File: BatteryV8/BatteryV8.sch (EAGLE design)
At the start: 69 parts, among them IC1 MAX6462XR29T, Q1 MOSFET-PCHANNEL, Q2 MOSFET-PCHANNEL, Q3 MOSFET-PCHANNEL, X1 MINI-USB-UX60-MB-5ST

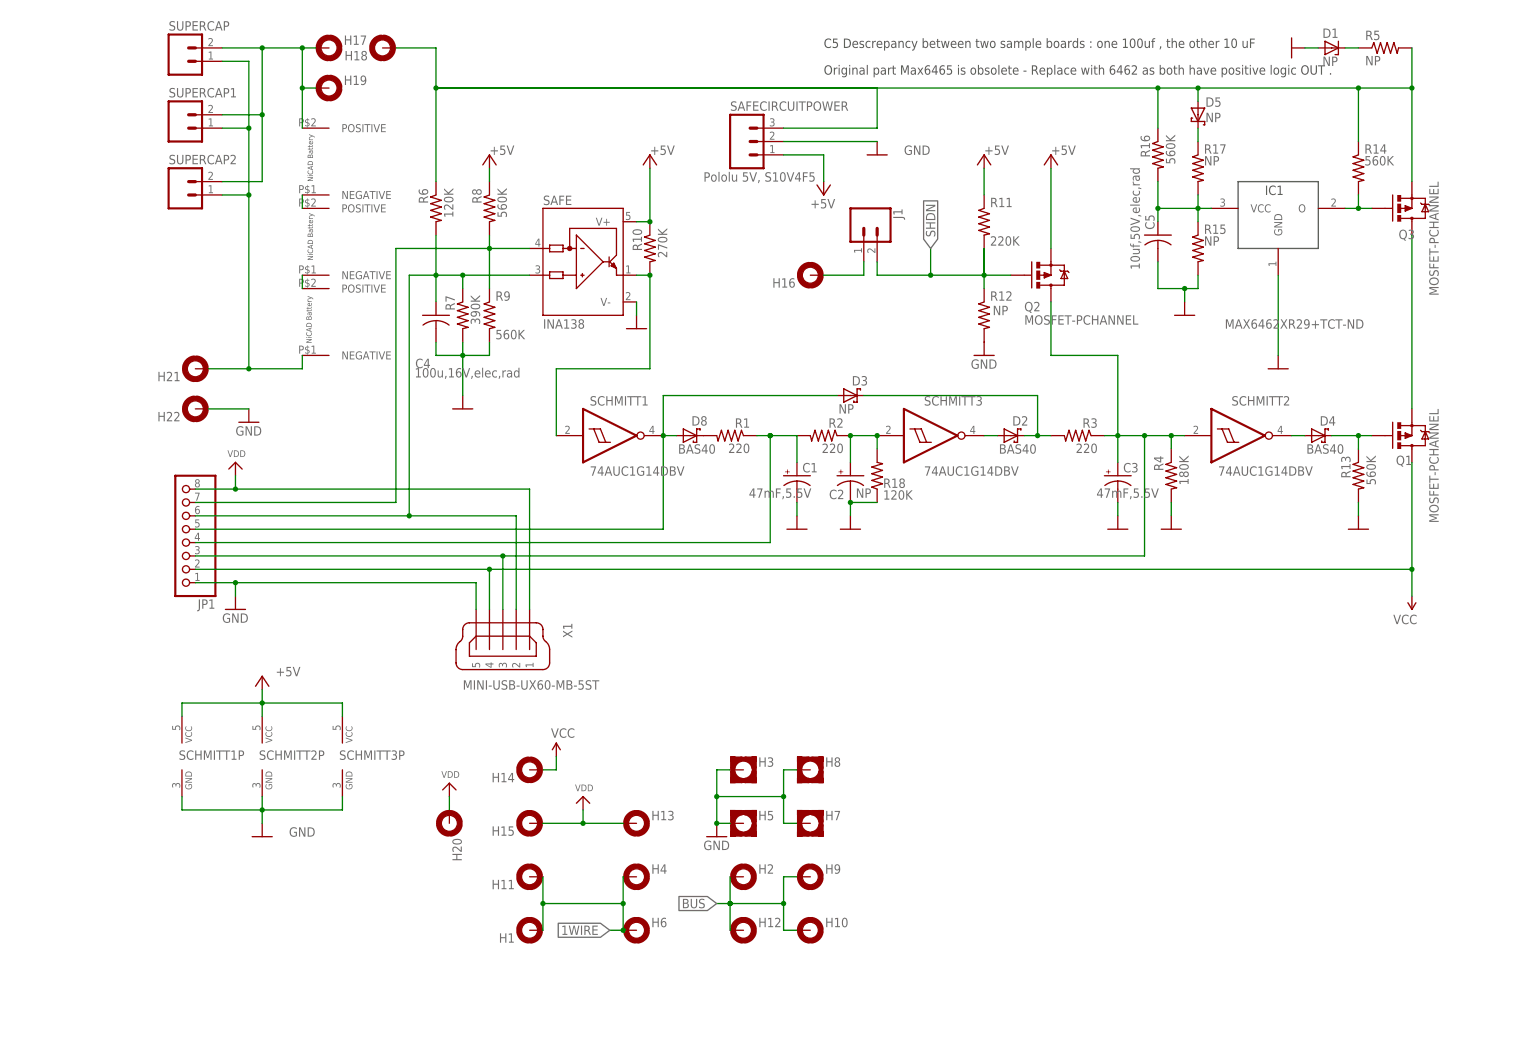
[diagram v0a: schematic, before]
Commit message: updated schematics and BOM with notes in the course of assembling the 3 main PCBs
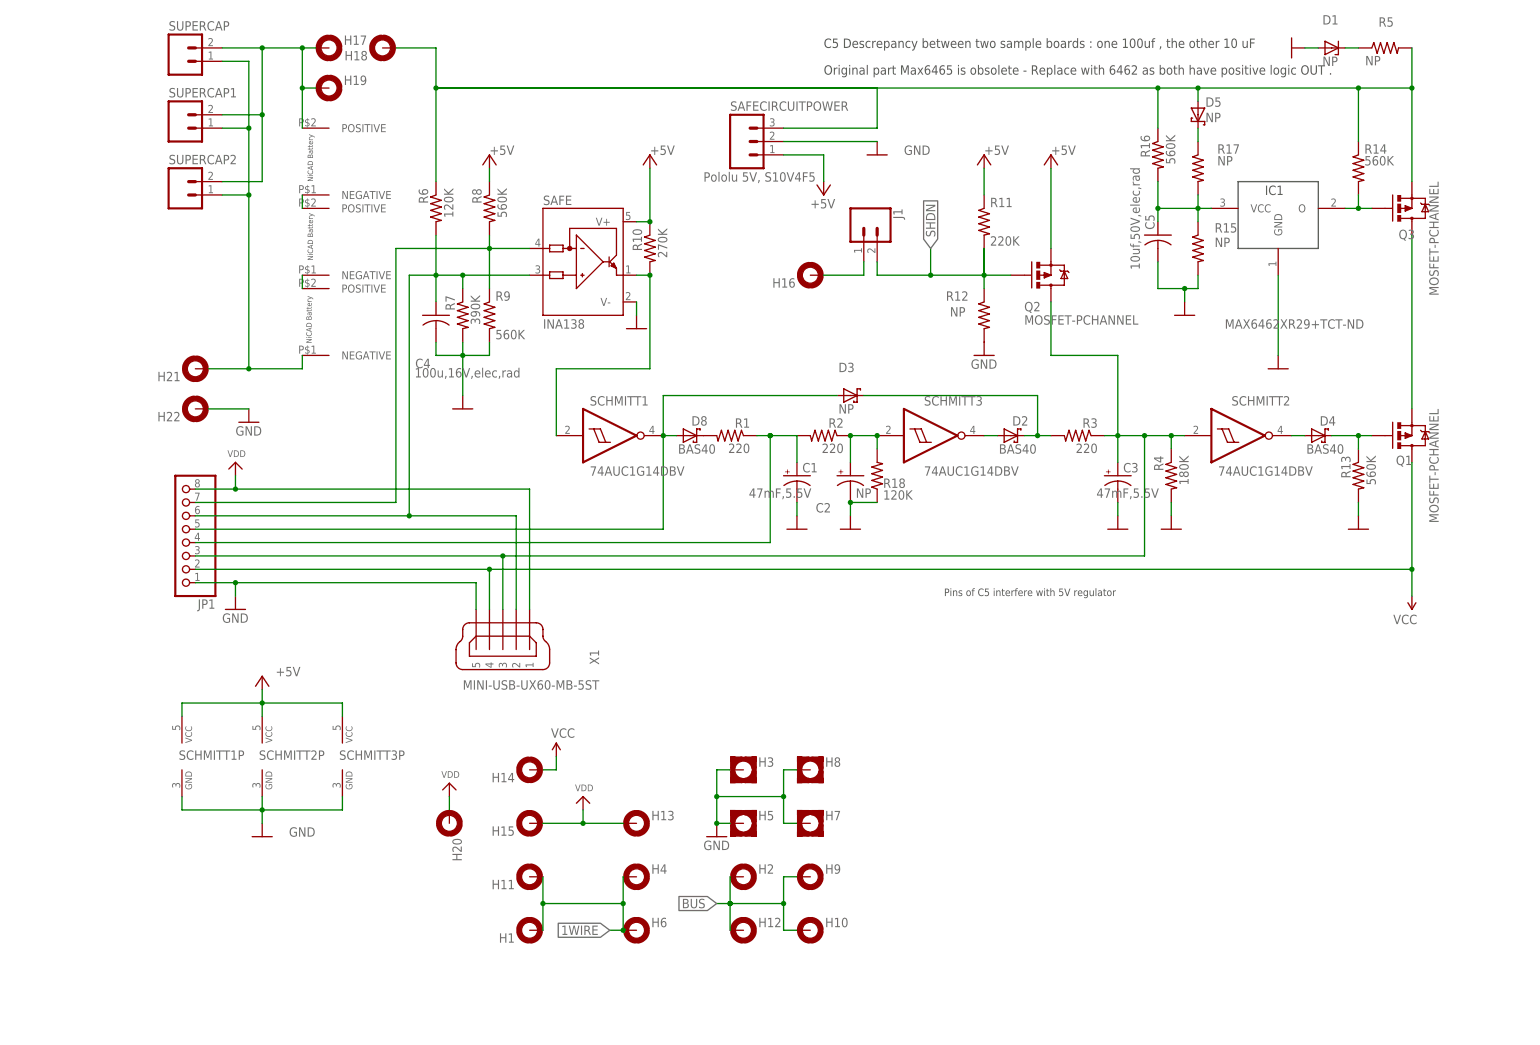
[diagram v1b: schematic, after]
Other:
- note added: "Pins of C5 interfere with 5V regulator"
- note removed: "Pins of C5 interfere with 3.3V regulator"
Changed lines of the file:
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@@
 <rectangle x1="53.34" y1="58.42" x2="81.28" y2="71.12" layer="117"/>
 <text x="149.86" y="68.58" size="1.4224" layer="117">Battery solder pads are too narrow for battery -- Potential for short on + </text>
-<text x="149.86" y="73.66" size="1.4224" layer="117">Pins of C5 interfere with 3.3V regulator</text>
+<text x="149.86" y="73.66" size="1.4224" layer="97">Pins of C5 interfere with 5V regulator</text>
 <text x="149.86" y="66.04" size="1.4224" layer="117">Add revision info to PCB</text>
 <text x="149.86" y="63.5" size="1.4224" layer="117">Footpringt for C4,C5 incorrect</text>
@@
 </instance>
 <instance part="C2" gate="G$1" x="132.08" y="96.52" smashed="yes">
-<attribute name="NAME" x="128.016" y="92.075" size="1.778" layer="95"/>
+<attribute name="NAME" x="125.476" y="89.535" size="1.778" layer="95"/>
 <attribute name="VALUE" x="133.096" y="92.329" size="1.778" layer="96"/>
 </instance>
@@
 </instance>
 <instance part="R12" gate="G$1" x="157.48" y="127" smashed="yes" rot="MR270">
-<attribute name="NAME" x="158.5976" y="129.7686" size="1.778" layer="95" rot="MR0" align="bottom-right"/>
-<attribute name="VALUE" x="159.1056" y="128.8034" size="1.778" layer="96" rot="MR0" align="top-right"/>
+<attribute name="NAME" x="150.2156" y="129.7686" size="1.778" layer="95" rot="MR0" align="bottom-right"/>
+<attribute name="VALUE" x="150.9776" y="128.5494" size="1.778" layer="96" rot="MR0" align="top-right"/>
 </instance>
 <instance part="+3V6" gate="G$1" x="157.48" y="157.48" smashed="yes"/>
 <instance part="X1" gate="G$1" x="66.04" y="66.04" smashed="yes" rot="R270">
-<attribute name="NAME" x="77.47" y="68.58" size="1.778" layer="95" rot="R270"/>
+<attribute name="NAME" x="82.55" y="63.5" size="1.778" layer="95" rot="R270"/>
 <attribute name="VALUE" x="58.42" y="55.88" size="1.778" layer="96"/>
 </instance>
@@
 <instance part="GND10" gate="1" x="58.42" y="109.22" smashed="yes"/>
 <instance part="R5" gate="G$1" x="233.68" y="177.8" smashed="yes">
-<attribute name="NAME" x="229.87" y="179.2986" size="1.778" layer="95"/>
+<attribute name="NAME" x="232.41" y="181.8386" size="1.778" layer="95"/>
 <attribute name="VALUE" x="229.87" y="174.498" size="1.778" layer="96"/>
 </instance>
 <instance part="D1" gate="1" x="223.52" y="177.8" smashed="yes">
-<attribute name="NAME" x="221.742" y="179.705" size="1.778" layer="95"/>
+<attribute name="NAME" x="221.742" y="182.245" size="1.778" layer="95"/>
 <attribute name="VALUE" x="221.742" y="174.371" size="1.778" layer="96"/>
 </instance>
@@
 </instance>
 <instance part="D3" gate="1" x="132.08" y="111.76" smashed="yes">
-<attribute name="NAME" x="132.334" y="113.665" size="1.778" layer="95"/>
+<attribute name="NAME" x="129.794" y="116.205" size="1.778" layer="95"/>
 <attribute name="VALUE" x="129.794" y="108.331" size="1.778" layer="96"/>
 <attribute name="DIGIKEY" x="132.08" y="111.76" size="1.778" layer="96" display="off"/>
@@
 </instance>
 <instance part="R15" gate="G$1" x="198.12" y="139.7" smashed="yes" rot="MR270">
-<attribute name="NAME" x="199.2376" y="142.4686" size="1.778" layer="95" rot="MR0" align="bottom-right"/>
-<attribute name="VALUE" x="199.2376" y="142.0114" size="1.778" layer="96" rot="MR0" align="top-right"/>
+<attribute name="NAME" x="201.2696" y="142.7226" size="1.778" layer="95" rot="MR0" align="bottom-right"/>
+<attribute name="VALUE" x="201.2696" y="141.7574" size="1.778" layer="96" rot="MR0" align="top-right"/>
 </instance>
 <instance part="C5" gate="G$1" x="190.5" y="142.24" smashed="yes">
@@
 </instance>
 <instance part="R17" gate="G$1" x="198.12" y="154.94" smashed="yes" rot="MR270">
-<attribute name="NAME" x="199.2376" y="157.7086" size="1.778" layer="95" rot="MR0" align="bottom-right"/>
-<attribute name="VALUE" x="199.2376" y="157.2514" size="1.778" layer="96" rot="MR0" align="top-right"/>
+<attribute name="NAME" x="201.7776" y="157.7086" size="1.778" layer="95" rot="MR0" align="bottom-right"/>
+<attribute name="VALUE" x="201.7776" y="157.2514" size="1.778" layer="96" rot="MR0" align="top-right"/>
 </instance>
 <instance part="J1" gate="G$1" x="134.62" y="144.78" smashed="yes" rot="R270">

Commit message: Modified schematic and BOM to represent actual board - Smitt triggers. Extracted library elements from schematic and created two local libraries with all the non standard or modified elements used on the board. Circuit analysis and write up of functional spec.
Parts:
- removed SAFECIRCUITPOWER: Pololu 5V, S10V4F5, SparkFun-Connectors:M03PTH
- added SAFECIRCUITPWR: (no value), pinhead:PINHD-1X3
- C1, C2, C3: device adafruit:CPOL-US153CLV-1010 -> rcl:CPOL-US153CLV-1010
- IC1: device EdgeCube:MAX6465 -> BatteryV8:EDGECUBE_MAX6465
- J1: device SparkFun-Connectors:CONN_02 -> pinhead:PINHD-1X2
- Q1, Q2, Q3: value MOSFET-PCHANNEL -> MOSFET P-CH; device SparkFun-DiscreteSemi:MOSFET-PCHANNEL -> SparkFun-DiscreteSemi:MOSFET_PCH-SI2309DS
- R1, R10, R11, R12, R13, R14, R15, R16, R17, R2, R3, R4, R6, R7, R8, R9: device adafruit:R-US_M0805 -> rcl:R-US_R0805
- R18: device rcl:R-US_0207/10 -> rcl:R-US_R0805
- R5: value NP -> 9999
- SCHMITT1: value 74AUC1G14DBV -> SN74LVC1G14DBVR; DIGIKET 296-12880-1-ND -> 296-11607-1-ND; TOPMARK C175 -> U14F,U14R
- SCHMITT2, SCHMITT3: value 74AUC1G14DBV -> 74LVC1G17DBV; device 74xx-little-us:74AUC1G14DBV -> 74xx-little-us:74LVC1G17DBV; DIGIKEY 296-12880-1-ND -> 296-11933-1-ND
- SUPERCAP, SUPERCAP1, SUPERCAP2: device SparkFun-Connectors:M02PTH -> pinhead:PINHD-1X2
- U$5, U$6, U$7: value AA-BATT -> JST-WATCH_AA-BATT; device JST-Watch:AA-BATT -> BatteryV8:JST-WATCH_AA-BATT
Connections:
- removed net N$22: D5.A, H18.MOUNT, Q3.S, R14.1, R16.1, R5.2, R6.1, SAFECIRCUITPOWER.3
- new net V-BATTERY: D5.A, H18.MOUNT, Q3.S, R14.1, R16.1, R5.2, R6.1, SAFECIRCUITPWR.3
- net +5V: now also SAFECIRCUITPWR.1; no longer SAFECIRCUITPOWER.1
- net GND: now also SAFECIRCUITPWR.2; no longer SAFECIRCUITPOWER.2
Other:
- note added: "A "Low" on Q1 closes the switch"
- note added: "A "Low" on Q3 closes the switch"
- note added: "C5 Discrepancy between two sample boards : one 100uf , the other 10 uF"
- note added: "Measured timing: C1: 6seconds /50 minutes C3: 6seconds/105 minutes C4: initial 12 seconds"
- note added: "Pololu 5V regulator"
- note added: "TC 12Sec"
- note added: "V-thresh 3.26V"
- note added: "normal op = high"
- note removed: "C5 Descrepancy between two sample boards : one 100uf , the other 10 uF"
- moved on the sheet: H14, H18, H20, J1, SUPERCAP, SUPERCAP1, SUPERCAP2
